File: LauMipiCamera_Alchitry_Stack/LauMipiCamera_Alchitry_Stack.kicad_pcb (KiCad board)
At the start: 4 copper layers, 55 x 45 mm, 19 parts, among them J1 DF40C-50DP (Site A / +3V3 onl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, J2 DF40C-80DP (Bank A / Site B /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, J3 DF40C-80DP (Bank B / Site C), SW1 SW_DIP_x4

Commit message: hw(mipi): explicit GND returns for SW1 and C1/C2; trim J1 +3V3 to 3 contacts
GND ties (13 segments, 5 vias). Both loads now have a dedicated copper return to
a DF40 ground pin, rather than relying on the pour alone -- and they return to
DIFFERENT connectors, so the paths are genuinely separate:

  * SW1's four GND pads -> short F.Cu stubs west to a B.Cu spine at x=133.5,
    then east under the board to J3 pad 2 (GND, 149.745/100.057), entering from
    the north as even-row pads require.
    The spine cannot run at x=135.305 (through the pads) because SW_BLUE and
    SW_RED thread the gaps between those same GND pads at y=93.46 and y=99.0.
  * C1/C2 GND pads -> F.Cu around the caps' own +3V3 pads, east at y=71.5, then
    a via down into J2 pad 1 (GND, 149.745/65.767).

J1 +3V3: 1/3/5/9/11 -> 1/3/5.

  Hirose DF40 contacts are rated 0.3 A each. The camera draws ~260 mA, so ONE
  pin (the fabricated trigger board's choice) sits at 87% of rating with no
  headroom for inrush. Three contacts give 0.9 A, a 3.5x margin, and cut the
  contact-resistance drop.

  Five was the wrong trade. ROADMAP asserts "+3V3 is on Site A odd pins 1-13"
  but its own open-items list (SS208.3) flags that map as needing
  re-confirmation, and warns "never wire VCC" (the even pins). No Br schematic
  is in the repo. Every additional pin tied is another opportunity to short
  +3V3 to a different rail if that map is wrong, for current margin we do not
  need. Pins 9 and 11 are now no-connects in both schematic and PCB.

  STILL GATED: confirm Site A's pin map against the Br schematic before fab.
  If it turns out only pin 1 is +3V3, this is a short.

DRC: 0 copper violations, schematic_parity 0. ERC: 1 (the known cached
Conn_01x22 symbol). SW1 and C1/C2 have no ratsnest left. Ratsnest 102 -> 96.

Co-Authored-By: Claude Opus 4.8 (1M context) <noreply@anthropic.com>
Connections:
- J1 pad 11: +3V3 -> unconnected-(J1-Pin_11-Pad11)
- J1 pad 9: +3V3 -> unconnected-(J1-Pin_9-Pad9)
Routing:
- net GND: track 0.00 -> 57.9 mm, vias 0 -> 5
- net +3V3: track 19.0 -> 16.5 mm
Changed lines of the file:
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@@
 			(layers "B.Cu" "B.Mask" "B.Paste")
 			(roundrect_rratio 0.25)
-			(net "+3V3")
+			(net "unconnected-(J1-Pin_9-Pad9)")
 			(pinfunction "Pin_9_9")
 			(pintype "passive")
@@
 			(layers "B.Cu" "B.Mask" "B.Paste")
 			(roundrect_rratio 0.25)
-			(net "+3V3")
+			(net "unconnected-(J1-Pin_11-Pad11)")
 			(pinfunction "Pin_11_11")
 			(pintype "passive")
@@
 	)
 	(segment
-		(start 132.8450 65.7670)
-		(end 132.8450 67.0000)
-		(width 0.2)
-		(layer "B.Cu")
-		(net "+3V3")
-	)
-	(segment
-		(start 133.2450 65.7670)
-		(end 133.2450 67.0000)
-		(width 0.2)
-		(layer "B.Cu")
-		(net "+3V3")
-	)
-	(segment
 		(start 131.2450 67.0000)
 		(end 134.5000 67.0000)
@@
 		(net "+3V3")
 	)
+	(segment
+		(start 135.3050 92.1900)
+		(end 133.5000 92.1900)
+		(width 0.25)
+		(layer "F.Cu")
+		(net "GND")
+	)
+	(segment
+		(start 135.3050 94.7300)
+		(end 133.5000 94.7300)
+		(width 0.25)
+		(layer "F.Cu")
+		(net "GND")
+	)
+	(segment
+		(start 135.3050 97.2700)
+		(end 133.5000 97.2700)
+		(width 0.25)
+		(layer "F.Cu")
+		(net "GND")
+	)
+	(segment
+		(start 135.3050 99.8100)
+		(end 133.5000 99.8100)
+		(width 0.25)
+		(layer "F.Cu")
+		(net "GND")
+	)
+	(segment
+		(start 133.5000 92.1900)
+		(end 133.5000 99.8100)
+		(width 0.25)
+		(layer "B.Cu")
+		(net "GND")
+	)
+	(segment
+		(start 133.5000 98.8000)
+		(end 149.7450 98.8000)
+		(width 0.25)
+		(layer "B.Cu")
+		(net "GND")
+	)
+	(segment
+		(start 149.7450 98.8000)
+		(end 149.7450 100.0570)
+		(width 0.25)
+		(layer "B.Cu")
+		(net "GND")
+	)
+	(segment
+		(start 132.9000 70.0000)
+		(end 132.9000 71.5000)
+		(width 0.25)
+		(layer "F.Cu")
+		(net "GND")
+	)
+	(segment
+		(start 132.9000 71.5000)
+		(end 137.9500 71.5000)
+		(width 0.25)
+		(layer "F.Cu")
+		(net "GND")
+	)
+	(segment
+		(start 137.9500 71.5000)
+		(end 137.9500 70.0000)
+		(width 0.25)
+		(layer "F.Cu")
+		(net "GND")
+	)
+	(segment
+		(start 137.9500 71.5000)
+		(end 149.7450 71.5000)
+		(width 0.25)
+		(layer "F.Cu")
+		(net "GND")
+	)
+	(segment
+		(start 149.7450 71.5000)
+		(end 149.7450 68.0000)
+		(width 0.25)
+		(layer "F.Cu")
+		(net "GND")
+	)
+	(segment
+		(start 149.7450 68.0000)
+		(end 149.7450 65.7670)
+		(width 0.25)
+		(layer "B.Cu")
+		(net "GND")
+	)
+	(via
+		(at 133.5000 92.1900)
+		(size 0.6)
+		(drill 0.3)
+		(layers "F.Cu" "B.Cu")
+		(net "GND")
+	)
+	(via
+		(at 133.5000 94.7300)
+		(size 0.6)
+		(drill 0.3)
+		(layers "F.Cu" "B.Cu")
+		(net "GND")
+	)
+	(via
+		(at 133.5000 97.2700)
+		(size 0.6)
+		(drill 0.3)
+		(layers "F.Cu" "B.Cu")
+		(net "GND")
+	)
+	(via
+		(at 133.5000 99.8100)
+		(size 0.6)
+		(drill 0.3)
+		(layers "F.Cu" "B.Cu")
+		(net "GND")
+	)
+	(via
+		(at 149.7450 68.0000)
+		(size 0.6)
+		(drill 0.3)
+		(layers "F.Cu" "B.Cu")
+		(net "GND")
+	)
 )

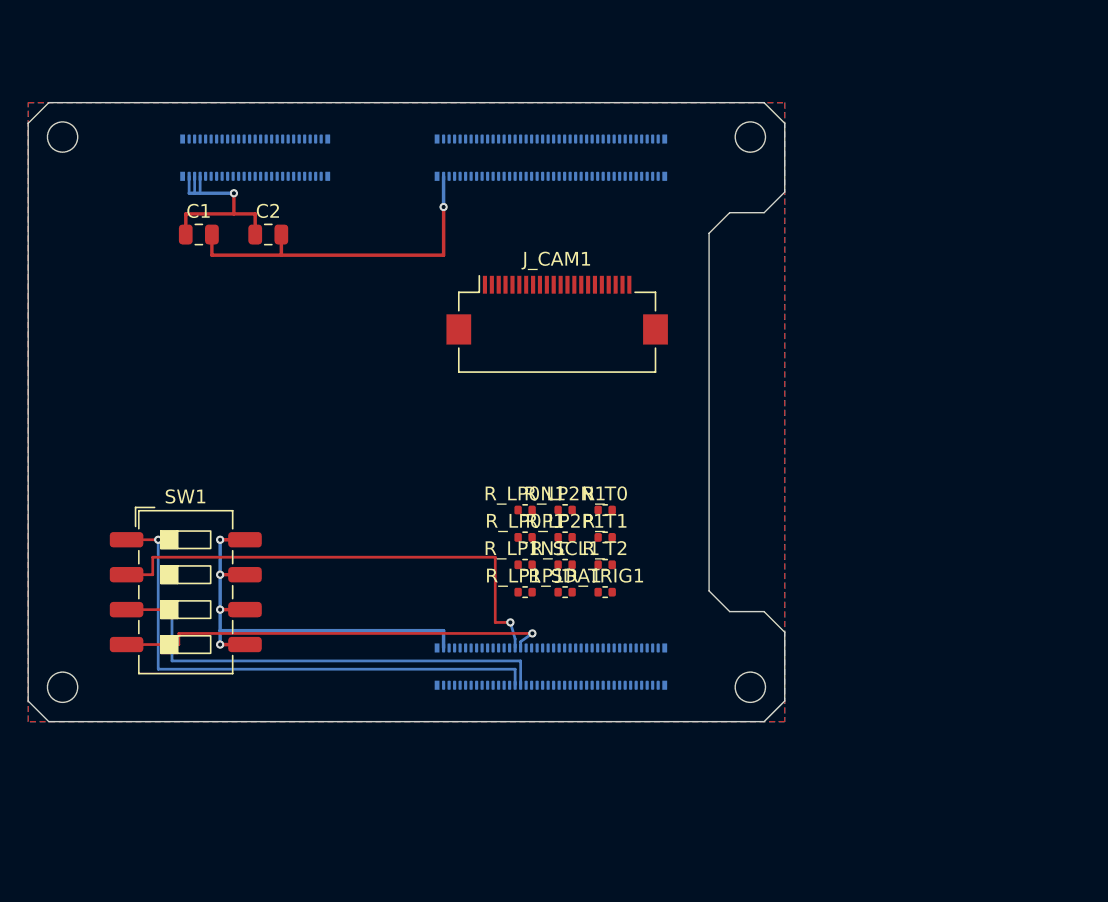
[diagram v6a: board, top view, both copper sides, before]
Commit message: hw(mipi): rip up routing and re-place footprints
Clears all 42 track segments and 10 vias so the components can be
re-placed from scratch; the 4 GND zones are kept. The board is
unrouted in this state - re-routing follows.

Co-Authored-By: Claude Opus 4.8 (1M context) <noreply@anthropic.com>
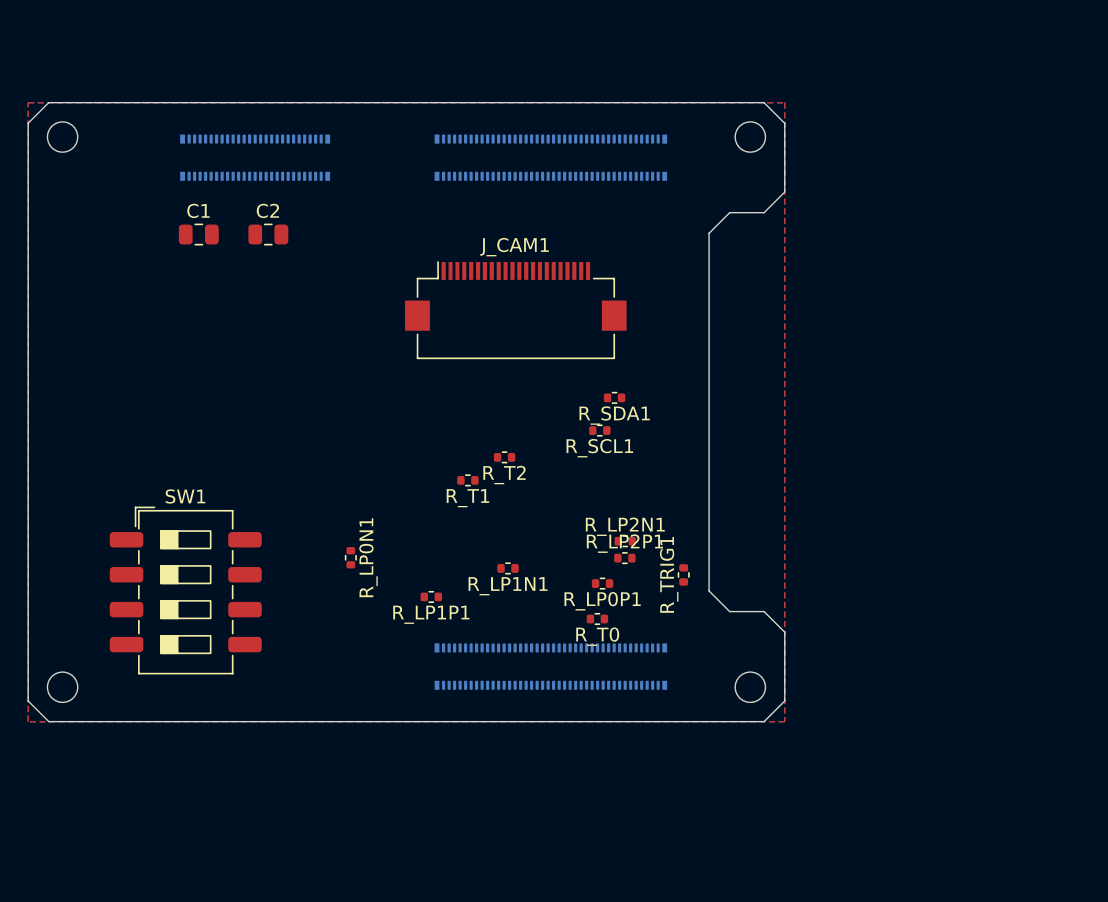
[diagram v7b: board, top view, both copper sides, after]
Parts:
- moved R_SDA1 14.6 mm to (162.2, 81.9), turned to 180 degrees
- moved R_LP0N1 13.1 mm to (143.0, 93.5), turned to -90 degrees
- moved R_T1 10.8 mm to (151.5, 87.9), turned to 180 degrees
- moved R_T2 10.7 mm to (154.2, 86.2), turned to 180 degrees
- moved R_SCL1 10.1 mm to (161.1, 84.2), turned to 180 degrees
- moved R_T0 7.94 mm to (160.9, 98.0), turned to 180 degrees
- moved R_LP1P1 6.83 mm to (148.8, 96.3), turned to 180 degrees
- moved R_LP0P1 6.55 mm to (161.3, 95.4), turned to 180 degrees
- moved R_TRIG1 5.85 mm to (167.2, 94.8), turned to 90 degrees
- moved R_LP2N1 4.92 mm to (162.9, 92.3)
- moved R_LP2P1 4.60 mm to (162.9, 93.5)
- moved J_CAM1 3.16 mm to (155.0, 74.5)
- moved R_LP1N1 1.27 mm to (154.4, 94.3), turned to 180 degrees
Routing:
- net GND: track 57.9 -> 0.00 mm, vias 5 -> 0
- net SW_HVSV: track 38.8 -> 0.00 mm, vias 1 -> 0
- net SW_BLUE: track 35.8 -> 0.00 mm, vias 1 -> 0
- net SW_GREEN: track 34.1 -> 0.00 mm, vias 1 -> 0
- net SW_RED: track 31.8 -> 0.00 mm, vias 1 -> 0
- net +3V3: track 16.5 -> 0.00 mm, vias 1 -> 0
